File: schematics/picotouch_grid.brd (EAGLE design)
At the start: 157.5 x 105.4 mm, 137 parts, among them K1 TOUCHKEYH, K10 TOUCHKEYH, K11 TOUCHKEYH, K12 TOUCHKEYH, K13 TOUCHKEYH, K14 TOUCHKEYH, K15 TOUCHKEYH, K16 TOUCHKEYH, K17 TOUCHKEYH, K18 TOUCHKEYH, K19 TOUCHKEYH, K2 TOUCHKEYH, K20 TOUCHKEYH, K21 TOUCHKEYH, K22 TOUCHKEYH, K23 TOUCHKEYH, K24 TOUCHKEYH, K25 TOUCHKEYH, K26 TOUCHKEYH, K27 TOUCHKEYH, K28 TOUCHKEYH, K29 TOUCHKEYH, K3 TOUCHKEYH, K30 TOUCHKEYH, K31 TOUCHKEYH, K32 TOUCHKEYH, K33 TOUCHKEYH, K34 TOUCHKEYH, K35 TOUCHKEYH, K36 TOUCHKEYH, K37 TOUCHKEYH, K38 TOUCHKEYH, K39 TOUCHKEYH, K4 TOUCHKEYH, K40 TOUCHKEYH, K5 TOUCHKEYH, K6 TOUCHKEYH, K7 TOUCHKEYH, K8 TOUCHKEYH, K9 TOUCHKEYH, U1 RASPBERRY_PICOSMD

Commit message: more grid idea
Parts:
- removed J2: (no value), SparkFun-Connectors:1X04
- added CONN1: STEMMA_I2C_QT, adafruit_electromech:JST_SH4
- added J3: AUDIO-JACK-TRRS, audio_jacks_todbot:PJ-320D_SPARKFUN
- added R15: 1.8k, rcl:R0805
- added R17: 220, rcl:R0805
- moved J1 2.54 mm to (61.0, 85.5)
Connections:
- new net MIDI_OUT: R17.2, U1.P$26
- new net N$38: J3.RING1, R15.1
- new net N$8: J3.TIP, R17.1
- net +3V3: now also CONN1.2, R15.2; no longer J2.2
- net GND: now also CONN1.1, J3.EARTH; no longer J2.1
- net SCL: now also CONN1.4; no longer J2.3
- net SDA: now also CONN1.3; no longer J2.4
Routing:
- net MIDI_OUT: track 0.00 -> 137.6 mm, vias 0 -> 2
- net +3V3: track 913.6 -> 993.5 mm, vias 6 -> 8
- net SDA: track 48.4 -> 74.5 mm
- net SCL: track 40.0 -> 61.2 mm
- net N$38: track 0.00 -> 12.1 mm
- net N$8: track 0.00 -> 6.65 mm
- net NEOPIXEL: track 23.2 -> 22.6 mm
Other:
- board text added: "https://github.com/todbot/picotouch"
- board text added: "optional I2C display R1-R40 - 1M C1-40 - 100n LED1-LED4 - SK6812MINI-E (rev. mount)"
- board text added: "picotouch_grid - capsense touch grid keyboard for Raspberry Pi Pico"
- board text removed: "R1-R14 - all 1M"
- board text removed: "https://github.com/todbot/keeboartouch"
- board text removed: "keeboartouch - capsense touch keyboard for KB2040 "Kee Boar""
- board text removed: "optional I2C OLED"

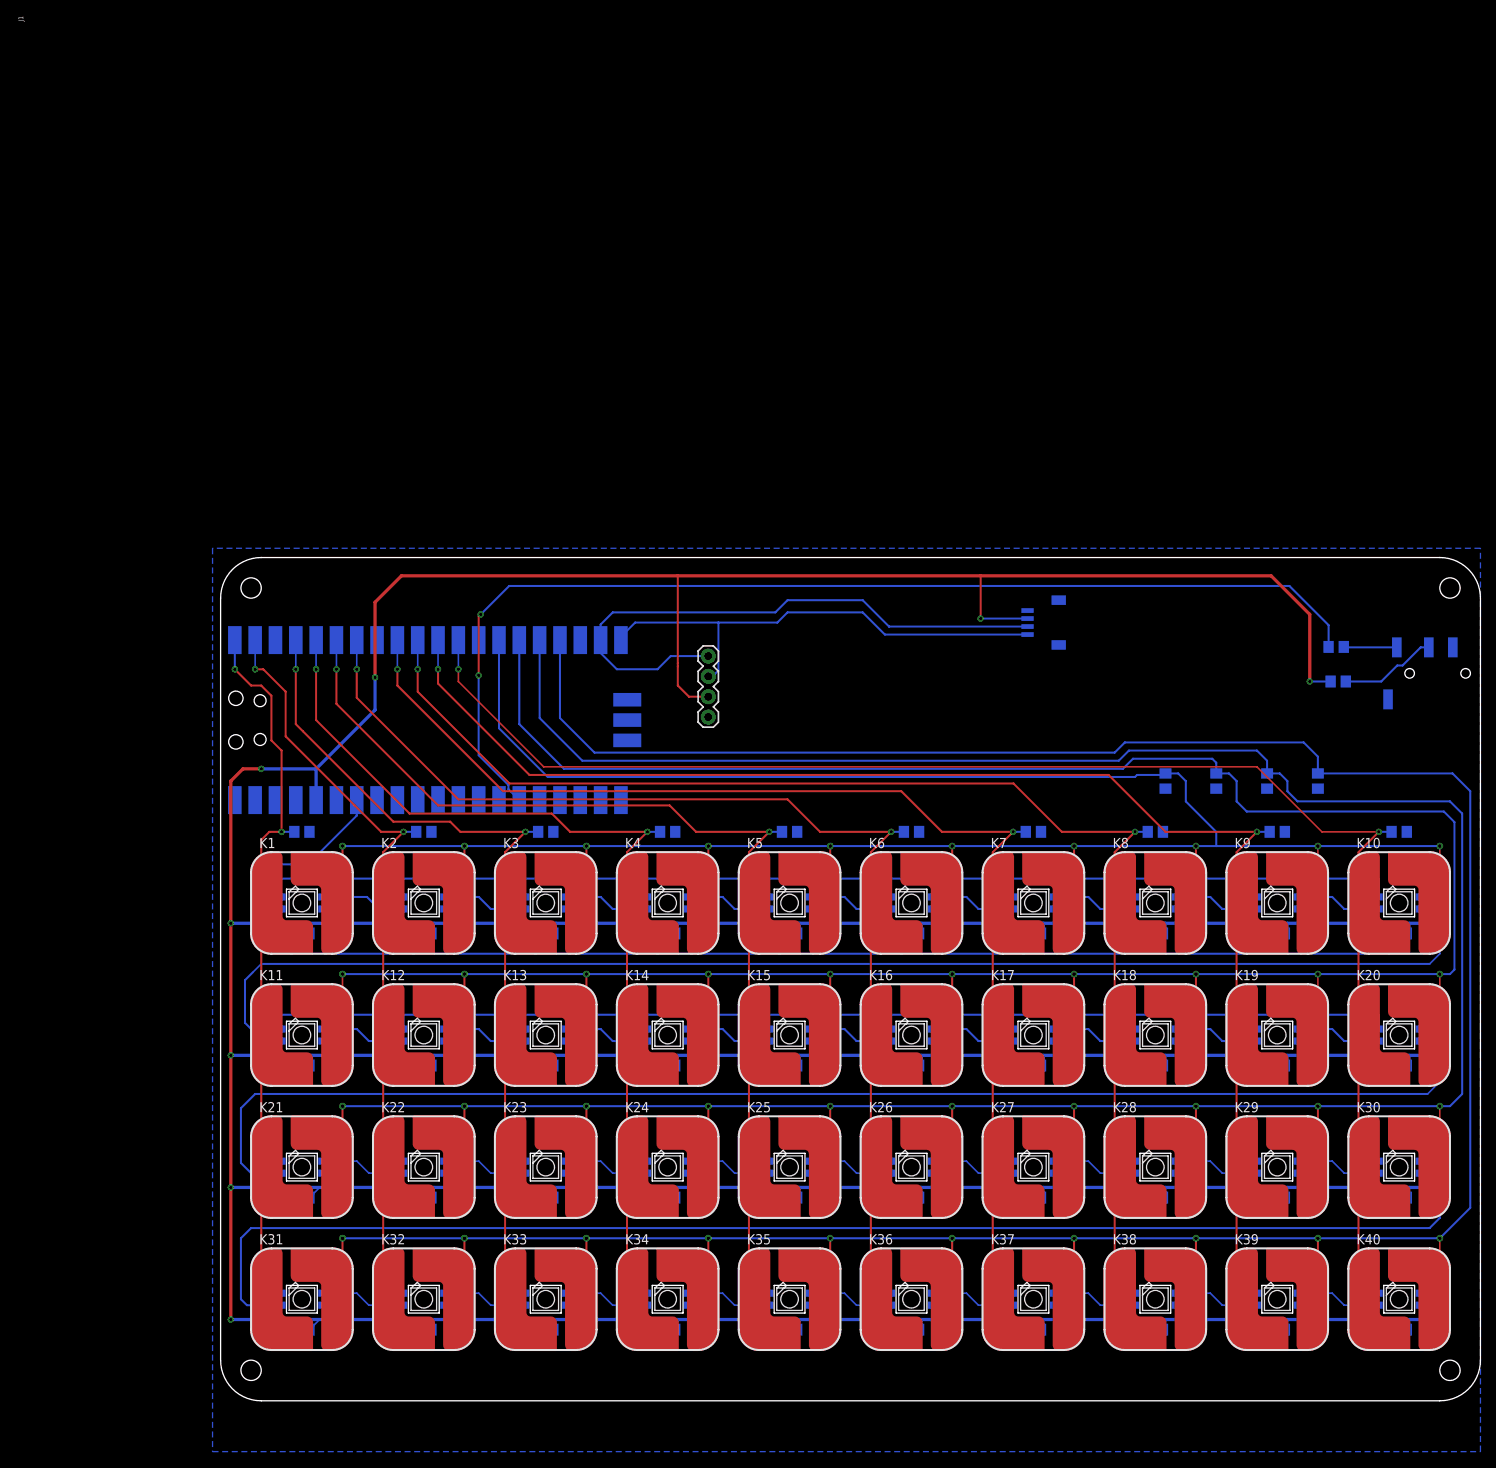
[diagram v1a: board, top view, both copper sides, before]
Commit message: grid idea has cutout now
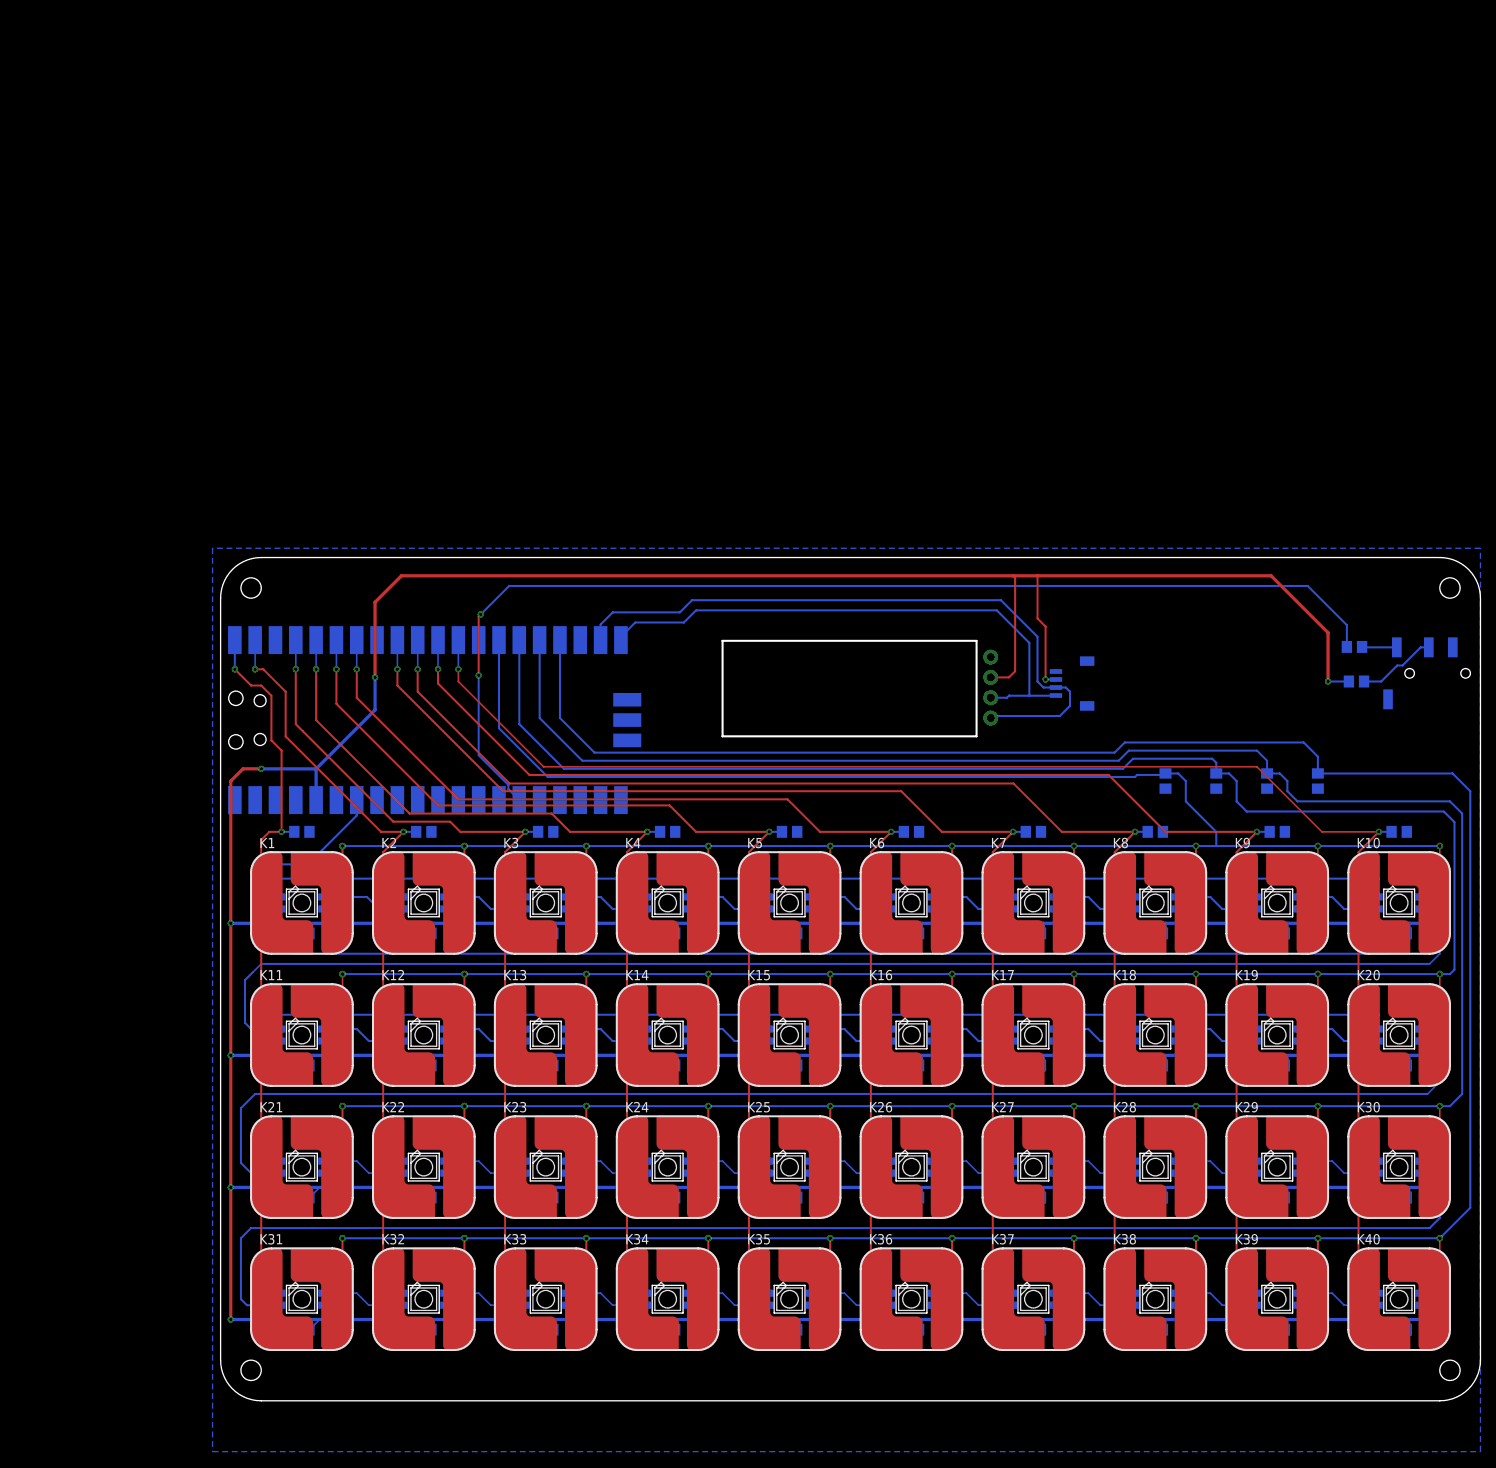
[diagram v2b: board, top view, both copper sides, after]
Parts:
- removed R17: 220, rcl:R0805
- added R16: 10, rcl:R0805
- R15: value 1.8k -> 33
- moved J1 36.1 mm to (96.3, 93.0), flipped to the bottom, turned to 270 degrees
- moved CONN1 8.41 mm to (106.4, 89.7)
- moved R15 2.29 mm to (142.0, 89.9)
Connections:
- net GND: now also CONN1.MT1, CONN1.MT2
- net MIDI_OUT: now also R16.2; no longer R17.2
- net N$8: now also R16.1; no longer R17.1
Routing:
- net SDA: track 74.5 -> 83.8 mm
- net SCL: track 61.2 -> 69.4 mm
- net N$8: track 6.65 -> 4.37 mm
- net N$38: track 12.1 -> 9.86 mm
- net MIDI_OUT: track 137.6 -> 139.9 mm
- net +3V3: track 993.5 -> 995.2 mm
- net GND: track 475.9 -> 474.7 mm
- net NEOPIXEL: track 22.6 -> 21.7 mm
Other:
- outline, holes or cut-outs redrawn
- board text added: "MIDI TRS-A OUT"
- board text added: "Qwiic / StemmaQT"
- board text added: "Raspberry Pi Pico"
- board text added: "https://github.com/todbot/picotouch 30 Jan 2023 - @todbot"
- board text added: "optional I2C display R1-R14 - 1M C1-40 - 100n R15 - 33, R16 - 10 LED1-LED40 - SK6812MINI-E (rev. mount)"
- board text removed: "30 Jan 2023 - @todbot"
- board text removed: "https://github.com/todbot/picotouch"
- board text removed: "optional I2C display R1-R40 - 1M C1-40 - 100n LED1-LED4 - SK6812MINI-E (rev. mount)"
